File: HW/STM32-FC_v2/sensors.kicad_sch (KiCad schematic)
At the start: 18 parts, among them J5 JST ZH 1.5mm 2P, U10 LPS22HH, U7 BMI323, U8 ICM-42688-P, U9 LIS2MDLTR

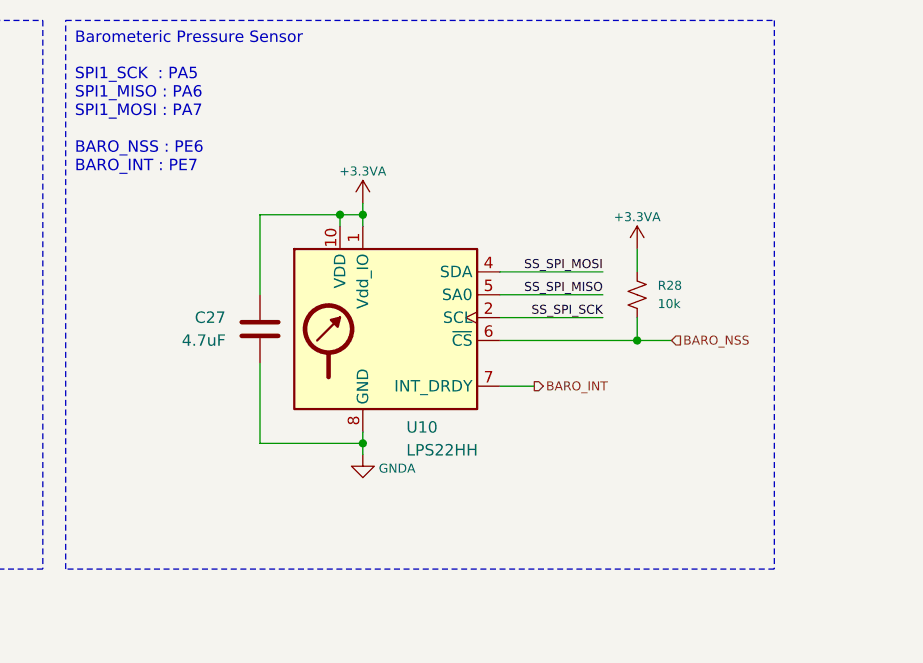
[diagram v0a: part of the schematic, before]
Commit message: LPS22HH Baro update(WIP) and Radio update
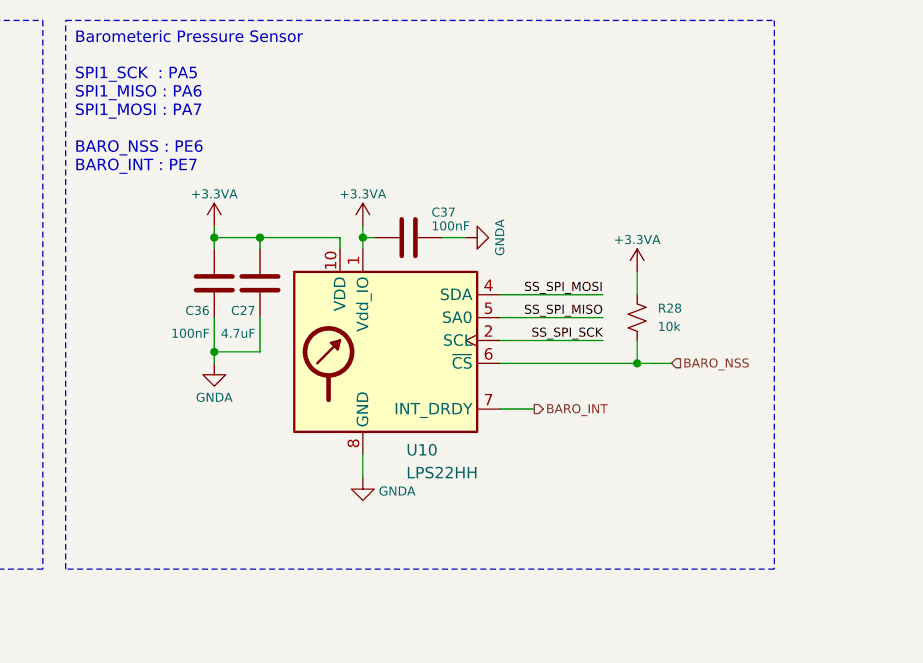
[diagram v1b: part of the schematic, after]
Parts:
- added C36, C37: 100nF, Capacitor_SMD:C_0402_1005Metric, symbol Device:C
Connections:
- net +3.3VA: now also C36.2, C37.2
- net GND: now also C36.1, C37.1
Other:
- moved on the sheet: C27, R28, U10
